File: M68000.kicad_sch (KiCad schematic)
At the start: 18 parts, among them J1 JTAG, U1 MAX232, U2 XC9572XL-VQ64, U3 MC68000FN, U5 68C681, X1 ECS-2200B-080

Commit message: All parts and begin schematics
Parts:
- removed J1: JTAG, Connector_PinHeader_2.54mm:PinHeader_1x05_P2.54mm_Vertical, symbol Connector:Conn_01x05_Male
- removed J?: DB9_Female_MountingHoles, Connector_Dsub:DSUB-9_Female_Horizontal_P2.77x2.84mm_EdgePinOffset7.70mm_Housed_MountingHolesOffset9.12mm, symbol Connector:DB9_Female_MountingHoles
- removed U1: MAX232, Package_DIP:DIP-16_W7.62mm_Socket, symbol Interface_UART:MAX232
- removed U2: XC9572XL-VQ64, Package_QFP:TQFP-64_10x10mm_P0.5mm, symbol CPLD_Xilinx:XC9572XL-VQ64
- removed U5: 68C681, Package_LCC:PLCC-44_SMD-Socket, symbol Interface_UART:68C681
- removed U?: AT28C256, Package_LCC:PLCC-32_11.4x14.0mm_P1.27mm, symbol Memory_EEPROM:28C256
- removed U? (x2): AS6C62256, Package_DIP:DIP-28_W15.24mm, symbol Memory_RAM:KM62256CLP
- removed X?: ECS-2100AX-036, Oscillator:Oscillator_DIP-8_LargePads, symbol Oscillator:CXO_DIP8
- added C? (x2): 1uF, Capacitor_SMD:C_0805_2012Metric_Pad1.18x1.45mm_HandSolder, symbol Device:C
- added J?: Conn_01x06_Male, Connector_PinHeader_2.54mm:PinHeader_1x06_P2.54mm_Vertical, symbol Connector:Conn_01x06_Male
- added R?: 4.7k, Resistor_SMD:R_0805_2012Metric_Pad1.20x1.40mm_HandSolder, symbol Device:R
- added U?: XC9572, Package_LCC:PLCC-84_THT-Socket, symbol CPLD_Xilinx:XC95108PC84
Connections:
- net VCC is gone; now on net +5V: U?.1 (VCC), U?.2 (VCC)
- net GND: now also X1.4 (GND), C?.1, C?.2, J?.5 (Pin_5)
- net +5V: now reaches U3.14 (VCC)
- net +5V: now also U3.52 (VCC), X1.8 (Vcc), C?.1, C?.2, J?.6 (Pin_6), R?.2, U?.22 (VCCIO), U?.38 (VCC), U?.64 (VCCIO), U?.73 (VCC), U?.78 (VCC)
- net at U3.15 (CLK): now also X1.5 (OUT)
- net at U?.7 (~{RESET}): now also R?.1
- new net TCK: J?.4 (Pin_4), U?.30 (TCK)
- new net TDI: J?.2 (Pin_2), U?.28 (TDI)
- new net TDO: J?.3 (Pin_3), U?.59 (TDO)
- new net TMS: J?.1 (Pin_1), U?.29 (TMS)
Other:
- added sheet Duart Serial Interface (serial.kicad_sch)
- added sheet Memory (memory.kicad_sch)
- moved on the sheet: C?, D?, R?, U3, U?

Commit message: Final PCB Layout
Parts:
- removed C?: 1uF, Capacitor_SMD:C_0805_2012Metric_Pad1.18x1.45mm_HandSolder, symbol Device:C
- removed D?: Green, LED_SMD:LED_0805_2012Metric_Pad1.15x1.40mm_HandSolder, symbol Device:LED_Small
- removed D?: Red, LED_SMD:LED_0805_2012Metric_Pad1.15x1.40mm_HandSolder, symbol Device:LED_Small
- removed R? (x2): 4.7k, Resistor_SMD:R_0805_2012Metric_Pad1.20x1.40mm_HandSolder, symbol Device:R
- removed R?: 330, Resistor_SMD:R_0805_2012Metric_Pad1.20x1.40mm_HandSolder, symbol Device:R
- added C1, C2, C3, C4, C5: 1uF, Capacitor_SMD:C_0805_2012Metric_Pad1.18x1.45mm_HandSolder, symbol Device:C_Small
- added C8: 100uF, Capacitor_SMD:C_1210_3225Metric_Pad1.33x2.70mm_HandSolder, symbol Device:C
- added D0, D1, D2, D3: Green, LED_SMD:LED_0805_2012Metric_Pad1.15x1.40mm_HandSolder, symbol Device:LED_Small
- added D12: PWR_LED, LED_SMD:LED_0805_2012Metric_Pad1.15x1.40mm_HandSolder, symbol Device:LED_Small
- added D4, D5, D6: Blue, LED_SMD:LED_0805_2012Metric_Pad1.15x1.40mm_HandSolder, symbol Device:LED_Small
- added FC0, FC1, FC2: Red, LED_SMD:LED_0805_2012Metric_Pad1.15x1.40mm_HandSolder, symbol Device:LED_Small
- added J2: USB_B, MCD Footprints:USB_Micro-B_CS5A-NF, symbol Connector:USB_B_Mini
- added JP1: Power Jumper, Connector_PinHeader_2.54mm:PinHeader_1x02_P2.54mm_Vertical, symbol Jumper:Jumper_2_Open
- added R1, R10, R11, R12, R13, R14, R15, R2, R20, R3, R4, R5, R6, R7, R8, R9: 330, Resistor_SMD:R_0805_2012Metric_Pad1.20x1.40mm_HandSolder, symbol Device:R
- added R16, R17, R18, R19: 4.7k, Resistor_SMD:R_0805_2012Metric_Pad1.20x1.40mm_HandSolder, symbol Device:R
- added SW1: Util_SW, Button_Switch_SMD:SW_DIP_SPSTx04_Slide_6.7x11.72mm_W8.61mm_P2.54mm_LowProfile, symbol Switch:SW_DIP_x04
- added SW2: RESET_SW, Button_Switch_THT:SW_PUSH_6mm, symbol Switch:SW_SPST
- added SW3: STEP_SW, Button_Switch_THT:SW_PUSH_6mm, symbol Switch:SW_SPST
- C6, C7: renamed from C?; symbol Device:C -> Device:C_Small
- J1: renamed from J?; value Conn_01x06_Male -> JTAG1; footprint Connector_PinHeader_2.54mm:PinHeader_1x06_P2.54mm_Vertical -> MCD Footprints:JTAG PinHeader_1x06_P2.54mm_Vertical
- U1: renamed from U?; value MAX699CPA -> MAX699; symbol Power_Supervisor:LM809 -> MCD_Symbols:MAX699; Name (none) -> Reset Supervisor
- U2: renamed from U?; Name (none) -> CPLD
- U3: Name (none) -> CPU
- X1: symbol Oscillator:CXO_DIP8 -> MCD_Symbols:ECS_CLK_DIP8
- gave numbers to parts that had none: 1
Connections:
- net +5V: now also C7.1, D7.2 (A), C1.1, C2.1, C3.2, C4.1, C5.1, D0.2 (A), D1.2 (A), D2.2 (A), D3.2 (A), D4.2 (A), D5.2 (A), D6.2 (A), JP1.2 (B), R16.1, R17.1, R18.1, R19.1, SW1.5, SW1.6, SW1.7, SW1.8; no longer C7.2
- net GND: now also C7.2, U2.16 (GND), U2.27 (GND), U2.42 (GND), U2.49 (GND), U2.60 (GND), U2.8 (GND), U3.16 (GND), U3.17 (GND), U3.56 (GND), U3.57 (GND), C1.2, C2.2, C3.1, C4.2, C5.2, C8.2, D12.1 (K), FC0.1 (K), FC1.1 (K), FC2.1 (K), J2.5 (GND), J2.6 (Shield), R1.1, R2.1, R3.1, R5.1, SW2.1 (A), SW3.1 (A); no longer C7.1
- net at D7.1 (K): now also R8.1
- net 699_~{RESET}: now reaches U1.7 (~{RESET})
- net 699_~{RESET}: now also U2.1 (P1)
- net D4: now reaches U3.1 (D4)
- net CPU_~{DTACK}: now reaches U3.10 (~{DTACK})
- net CPU_~{DTACK}: now also U2.44 (P44)
- net ~{BGACK}: now reaches U3.12 (~{BGACK})
- net ~{BGACK}: now also U2.45 (P45)
- net ~{BR}: now reaches U3.13 (~{BR})
- net ~{BR}: now also U2.43 (P43)
- net 8Mhz CLK: now reaches X1.5 (OUT)
- net 8Mhz CLK: now also U2.32 (P32); no longer U3.15 (CLK)
- net CPU_~{HALT}: now reaches U3.19 (~{HALT})
- net CPU_~{HALT}: now also U2.41 (P41), R17.2
- net D3: now reaches U3.2 (D3)
- net CPU_~{RESET}: now reaches U3.20 (~{RESET})
- net CPU_~{RESET}: now also U2.46 (P46), R16.2
- net ~{VPA}: now reaches U3.23 (~{VPA})
- net ~{VPA}: now also U2.47 (P47)
- net CPU_~{BERR}: now reaches U3.24 (~{BERR})
- net CPU_~{BERR}: now also U2.31 (P31)
- net CPU_~{IPL2}: now reaches U3.25 (~{IPL2})
- net CPU_~{IPL2}: now also U2.39 (P39)
- net CPU_~{IPL1}: now reaches U3.26 (~{IPL1})
- net CPU_~{IPL1}: now also U2.37 (P37)
- net CPU_~{IPL0}: now reaches U3.27 (~{IPL0})
- net CPU_~{IPL0}: now also U2.35 (P35)
- net CPU_FC2: now reaches U3.28 (FC2)
- net CPU_FC2: now also U2.33 (P33)
- net CPU_FC1: now reaches U3.29 (FC1)
- net CPU_FC1: now also U2.36 (P36)
- net D2: now reaches U3.3 (D2)
- net CPU_FC0: now reaches U3.30 (FC0)
- net CPU_FC0: now also U2.34 (P34)
- net A1: now reaches U3.32 (A1)
- net A2: now reaches U3.33 (A2)
- net A3: now reaches U3.34 (A3)
- net A4: now reaches U3.35 (A4)
- net A5: now reaches U3.36 (A5)
- net A6: now reaches U3.37 (A6)
- net A7: now reaches U3.38 (A7)
- net A8: now reaches U3.39 (A8)
- net D1: now reaches U3.4 (D1)
- net A9: now reaches U3.40 (A9)
- net A10: now reaches U3.41 (A10)
- net A11: now reaches U3.42 (A11)
- net A12: now reaches U3.43 (A12)
- net A13: now reaches U3.44 (A13)
- net A14: now reaches U3.45 (A14)
- net A15: now reaches U3.46 (A15)
- net A16: now reaches U3.47 (A16)
- net A16: now also U2.26 (P26)
- net A17: now reaches U3.48 (A17)
- net A17: now also U2.24 (P24)
- net A18: now reaches U3.49 (A18)
- net A18: now also U2.25 (P25)
- net D0: now reaches U3.5 (D0)
- net A19: now reaches U3.50 (A19)
- net A19: now also U2.23 (P23)
- net A20: now reaches U3.51 (A20)
- net A21: now reaches U3.53 (A21)
- net A22: now reaches U3.54 (A22)
- net A23: now reaches U3.55 (A23)
- net D15: now reaches U3.58 (D15)
- net D14: now reaches U3.59 (D14)
- net CPU_~{AS}: now reaches U3.6 (~{AS})
- net CPU_~{AS}: now also U2.17 (P17)
- net D13: now reaches U3.60 (D13)
- net D12: now reaches U3.61 (D12)
- net D11: now reaches U3.62 (D11)
- net D10: now reaches U3.63 (D10)
- net D9: now reaches U3.64 (D9)
- net D8: now reaches U3.65 (D8)
- net D7: now reaches U3.66 (D7)
- net D6: now reaches U3.67 (D6)
- net D5: now reaches U3.68 (D5)
- net CPU_~{UDS}: now reaches U3.7 (~{UDS})
- net CPU_~{UDS}: now also U2.14 (P14)
- net CPU_~{LDS}: now reaches U3.8 (~{LDS})
- net CPU_~{LDS}: now also U2.15 (P15)
- net R/~{W}: now reaches U3.9 (R/~{W})
- net R/~{W}: now also U2.21 (P21)
- net DUART_~{RESET}: now reaches U2.10 (I/O/GCK2)
- net DUART_~{IACK}: now reaches U2.11 (P11)
- net RAM1_~{CS}: now reaches U2.12 (I/O/GCK3)
- net RAM2_~{CS}: now reaches U2.13 (P13)
- net ROM2_~{CS}: now reaches U2.18 (P18)
- net ROM1_~{CS}: now reaches U2.19 (P19)
- net MEM_~{OE}: now reaches U2.20 (P20)
- net DUART_~{CS}: now reaches U2.5 (P5)
- net at U2.51 (P51): now also R6.2
- net at U2.52 (P52): now also R4.2
- net at U2.53 (P53): now also R7.2
- net DUART_~{INT}: now reaches U2.6 (P6)
- net at U2.62 (P62): now also R8.2
- net at U2.63 (P63): now also R9.2
- net at U2.65 (P65): now also R10.2
- net at U2.66 (P66): now also R11.2
- net at U2.67 (P67): now also R12.2
- net at U2.68 (P68): now also R13.2
- net at U2.69 (P69): now also R14.2
- net DUART_~{DTACK}: now reaches U2.7 (P7)
- net at U2.70 (P70): now also R15.2
- net at U2.79 (P79): now also R2.2, SW1.3
- net at U2.80 (P80): now also R1.2, SW1.4
- net at U2.81 (P81): now also R5.2, SW1.1
- net at U2.82 (P82): now also R3.2, SW1.2
- net SW_UTIL: now reaches U2.83 (P83)
- net SW_UTIL: now also R18.2, SW2.2 (B)
- net SW_RESET: now reaches U2.84 (P84)
- net SW_RESET: now also R19.2, SW3.2 (B)
- net CPU_CLK: now reaches U2.9 (I/O/GCK1)
- net CPU_CLK: now also U3.15 (CLK)
- new net: D2.1 (K), R13.1
- new net: D0.1 (K), R15.1
- new net: D12.2 (A), R20.1
- new net: D6.1 (K), R9.1
- new net: FC0.2 (A), R4.1
- new net: D1.1 (K), R14.1
- new net: D4.1 (K), R11.1
- new net: D3.1 (K), R12.1
- new net: FC1.2 (A), R6.1
- new net: D5.1 (K), R10.1
- new net: FC2.2 (A), R7.1
- new net USB_POWER: C8.1, J2.1 (VBUS), JP1.1 (A), R20.2
- no-connect marks 0 -> 25
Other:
- sheet Duart Serial Interface ports: added A[1..4], DUART_~{DTACK}, DUART_~{IACK}, DUART_~{INT}, DUART_~{RESET}, R/~{W}; removed DUART_A[1..4], ~{DTACK}, ~{R/W}
- sheet Memory ports: added A[1..15], D[0..15]; removed A[0..14], D[0..7]
- note added: "General LEDs"
- note added: "USB Power Supply"
- moved on the sheet: C6, C7, D7, J1, U1, U2, U3, X1

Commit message: Submitted to JLCPCB
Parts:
- R1, R2, R3, R5: value 330 -> 4.7k
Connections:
- no-connect marks 25 -> 24
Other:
- moved on the sheet: C1, C2, C3, C4, C5, C6, C7, C8, D0, D1, D12, D2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

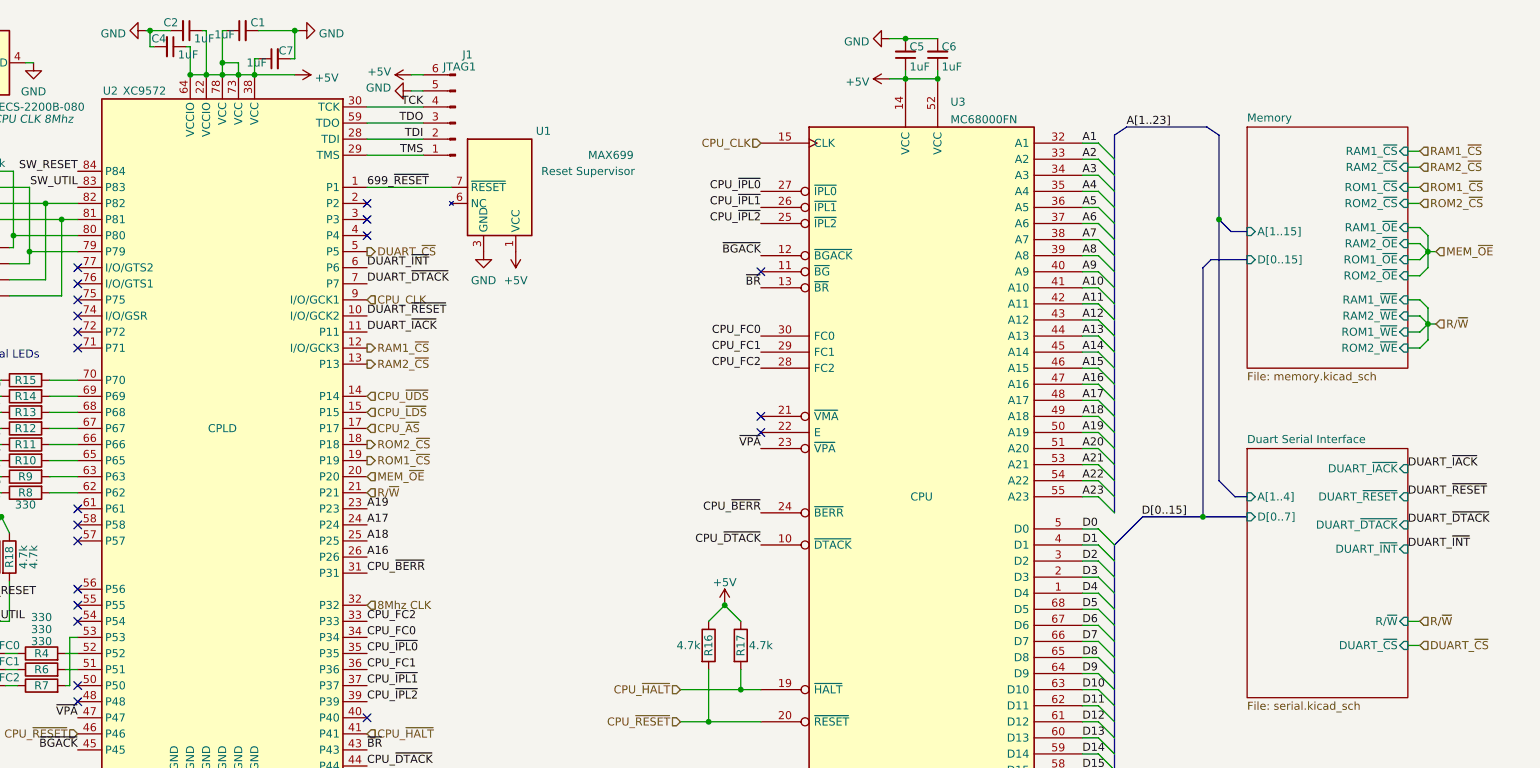
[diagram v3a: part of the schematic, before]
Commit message: Rename Memory to match High/Low
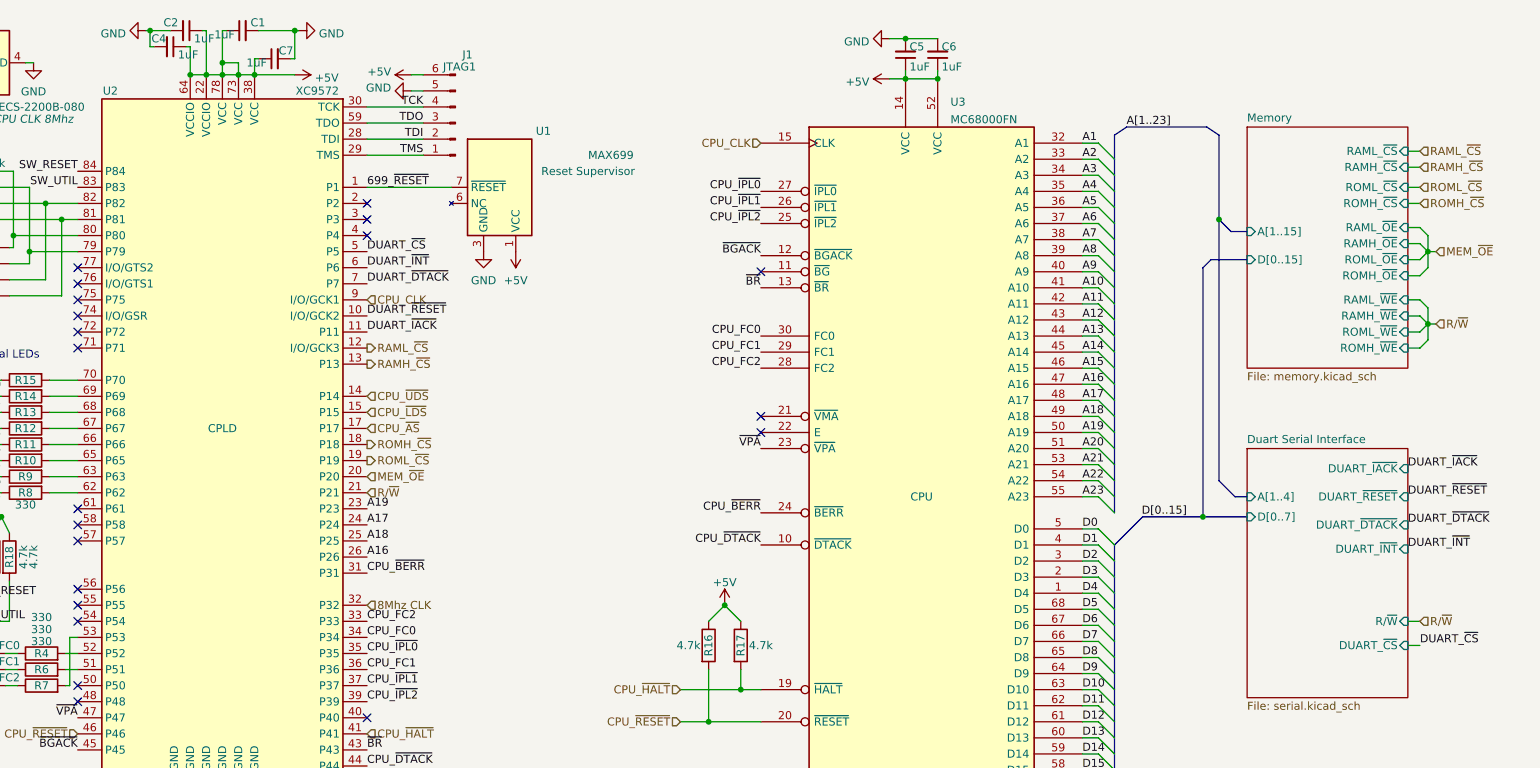
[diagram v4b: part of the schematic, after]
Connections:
- net RAM1_~{CS} renamed RAML_~{CS}
- net RAM2_~{CS} renamed RAMH_~{CS}
- net ROM1_~{CS} renamed ROML_~{CS}
- net ROM2_~{CS} renamed ROMH_~{CS}
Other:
- sheet Memory ports: added RAMH_~{CS}, RAMH_~{OE}, RAMH_~{WE}, RAML_~{CS}, RAML_~{OE}, RAML_~{WE}, ROMH_~{CS}, ROMH_~{OE}, ROMH_~{WE}, ROML_~{CS}, ROML_~{OE}, ROML_~{WE}; removed RAM1_~{CS}, RAM1_~{OE}, RAM1_~{WE}, RAM2_~{CS}, RAM2_~{OE}, RAM2_~{WE}, ROM1_~{CS}, ROM1_~{OE}, ROM1_~{WE}, ROM2_~{CS}, ROM2_~{OE}, ROM2_~{WE}
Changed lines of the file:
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@@
+    (effects (font (size 1.27 1.27)) (justify left bottom))
+  )
+  (label "DUART_~{CS}" (at 105.41 52.705 0)
     (effects (font (size 1.27 1.27)) (justify left bottom))
   )
@@
     (effects (font (size 1.27 1.27)) (justify left bottom))
   )
+  (label "DUART_~{CS}" (at 271.78 114.935 0)
+    (effects (font (size 1.27 1.27)) (justify left bottom))
+  )
   (label "TDI" (at 114.3 34.925 180)
     (effects (font (size 1.27 1.27)) (justify right bottom))
@@
     (effects (font (size 1.27 1.27)) (justify left))
   )
-  (hierarchical_label "RAM1_~{CS}" (shape output) (at 105.41 67.945 0)
+  (hierarchical_label "RAML_~{CS}" (shape output) (at 105.41 67.945 0)
     (effects (font (size 1.27 1.27)) (justify left))
   )
@@
     (effects (font (size 1.27 1.27)) (justify left))
   )
-  (hierarchical_label "ROM1_~{CS}" (shape input) (at 271.78 42.545 0)
-    (effects (font (size 1.27 1.27)) (justify left))
-  )
-  (hierarchical_label "DUART_~{CS}" (shape output) (at 105.41 52.705 0)
-    (effects (font (size 1.27 1.27)) (justify left))
-  )
-  (hierarchical_label "RAM2_~{CS}" (shape input) (at 271.78 39.37 0)
+  (hierarchical_label "ROML_~{CS}" (shape input) (at 271.78 42.545 0)
+    (effects (font (size 1.27 1.27)) (justify left))
+  )
+  (hierarchical_label "RAMH_~{CS}" (shape input) (at 271.78 39.37 0)
     (effects (font (size 1.27 1.27)) (justify left))
   )
@@
     (effects (font (size 1.27 1.27)) (justify left))
   )
-  (hierarchical_label "DUART_~{CS}" (shape input) (at 271.78 114.935 0)
-    (effects (font (size 1.27 1.27)) (justify left))
-  )
-  (hierarchical_label "RAM1_~{CS}" (shape input) (at 271.78 36.83 0)
+  (hierarchical_label "RAML_~{CS}" (shape input) (at 271.78 36.83 0)
     (effects (font (size 1.27 1.27)) (justify left))
   )
@@
     (effects (font (size 1.27 1.27)) (justify right))
   )
-  (hierarchical_label "ROM1_~{CS}" (shape output) (at 105.41 85.725 0)
+  (hierarchical_label "ROML_~{CS}" (shape output) (at 105.41 85.725 0)
     (effects (font (size 1.27 1.27)) (justify left))
   )
@@
     (effects (font (size 1.27 1.27)) (justify left))
   )
-  (hierarchical_label "ROM2_~{CS}" (shape input) (at 271.78 45.085 0)
-    (effects (font (size 1.27 1.27)) (justify left))
-  )
-  (hierarchical_label "RAM2_~{CS}" (shape output) (at 105.41 70.485 0)
+  (hierarchical_label "ROMH_~{CS}" (shape input) (at 271.78 45.085 0)
+    (effects (font (size 1.27 1.27)) (justify left))
+  )
+  (hierarchical_label "RAMH_~{CS}" (shape output) (at 105.41 70.485 0)
     (effects (font (size 1.27 1.27)) (justify left))
   )
@@
     (effects (font (size 1.27 1.27)) (justify left))
   )
-  (hierarchical_label "ROM2_~{CS}" (shape output) (at 105.41 83.185 0)
+  (hierarchical_label "ROMH_~{CS}" (shape output) (at 105.41 83.185 0)
     (effects (font (size 1.27 1.27)) (justify left))
   )
@@
       (effects (font (size 1.27 1.27)) (justify left))
     )
-    (property "Value" "XC9572" (id 1) (at 73.66 27.305 0)
+    (property "Value" "XC9572" (id 1) (at 100.965 27.305 0)
       (effects (font (size 1.27 1.27)) (justify left))
     )
@@
       (effects (font (size 1.27 1.27)) (justify left top))
     )
-    (pin "ROM1_~{CS}" input (at 269.875 42.545 0)
-      (effects (font (size 1.27 1.27)) (justify right))
-    )
-    (pin "ROM2_~{CS}" input (at 269.875 45.085 0)
-      (effects (font (size 1.27 1.27)) (justify right))
-    )
-    (pin "ROM1_~{WE}" input (at 269.875 65.405 0)
-      (effects (font (size 1.27 1.27)) (justify right))
-    )
-    (pin "ROM2_~{WE}" input (at 269.875 67.945 0)
-      (effects (font (size 1.27 1.27)) (justify right))
-    )
-    (pin "ROM1_~{OE}" input (at 269.875 53.975 0)
-      (effects (font (size 1.27 1.27)) (justify right))
-    )
-    (pin "ROM2_~{OE}" input (at 269.875 56.515 0)
-      (effects (font (size 1.27 1.27)) (justify right))
-    )
-    (pin "RAM1_~{CS}" input (at 269.875 36.83 0)
-      (effects (font (size 1.27 1.27)) (justify right))
-    )
-    (pin "RAM1_~{OE}" input (at 269.875 48.895 0)
-      (effects (font (size 1.27 1.27)) (justify right))
-    )
-    (pin "RAM1_~{WE}" input (at 269.875 60.325 0)
-      (effects (font (size 1.27 1.27)) (justify right))
-    )
-    (pin "RAM2_~{CS}" input (at 269.875 39.37 0)
-      (effects (font (size 1.27 1.27)) (justify right))
-    )
-    (pin "RAM2_~{WE}" input (at 269.875 62.865 0)
-      (effects (font (size 1.27 1.27)) (justify right))
-    )
-    (pin "RAM2_~{OE}" input (at 269.875 51.435 0)
-      (effects (font (size 1.27 1.27)) (justify right))
-    )
+    (pin "ROML_~{CS}" input (at 269.875 42.545 0)
+      (effects (font (size 1.27 1.27)) (justify right))
+    )
+    (pin "ROMH_~{CS}" input (at 269.875 45.085 0)
+      (effects (font (size 1.27 1.27)) (justify right))
+    )
+    (pin "ROML_~{WE}" input (at 269.875 65.405 0)
+      (effects (font (size 1.27 1.27)) (justify right))
+    )
+    (pin "ROMH_~{WE}" input (at 269.875 67.945 0)
+      (effects (font (size 1.27 1.27)) (justify right))
+    )
+    (pin "ROML_~{OE}" input (at 269.875 53.975 0)
+      (effects (font (size 1.27 1.27)) (justify right))
+    )
+    (pin "ROMH_~{OE}" input (at 269.875 56.515 0)
+      (effects (font (size 1.27 1.27)) (justify right))
+    )
+    (pin "RAML_~{CS}" input (at 269.875 36.83 0)
+      (effects (font (size 1.27 1.27)) (justify right))
+    )
+    (pin "RAML_~{OE}" input (at 269.875 48.895 0)
+      (effects (font (size 1.27 1.27)) (justify right))
+    )
+    (pin "RAML_~{WE}" input (at 269.875 60.325 0)
+      (effects (font (size 1.27 1.27)) (justify right))
+    )
+    (pin "RAMH_~{CS}" input (at 269.875 39.37 0)
+      (effects (font (size 1.27 1.27)) (justify right))
+    )
+    (pin "RAMH_~{WE}" input (at 269.875 62.865 0)
+      (effects (font (size 1.27 1.27)) (justify right))
+    )
+    (pin "RAMH_~{OE}" input (at 269.875 51.435 0)
+      (effects (font (size 1.27 1.27)) (justify right))
+    )

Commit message: PCB v1 final design
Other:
- moved on the sheet: C8, D12, J2, JP1, R20
